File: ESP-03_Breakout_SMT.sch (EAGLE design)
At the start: 3 parts

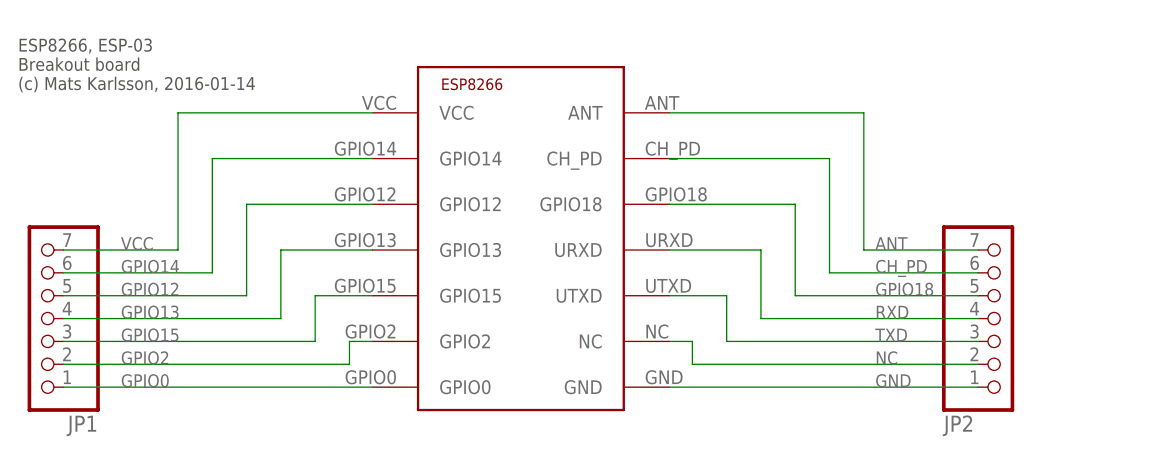
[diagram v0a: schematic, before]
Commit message: Minor cosmetic changes
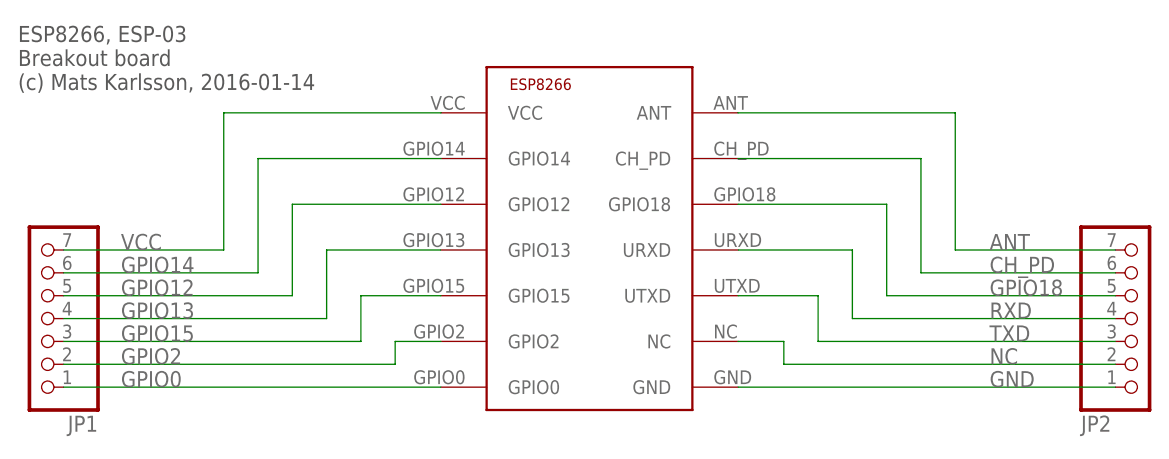
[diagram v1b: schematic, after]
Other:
- moved on the sheet: JP2
